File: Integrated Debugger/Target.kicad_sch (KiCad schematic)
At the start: 10 parts, among them J3 FPC socket 10P, J4 20021521-00010T1LF, Q1 DMN31D5UDA-7B, SW5 RESET, U3 TXB0106RGY

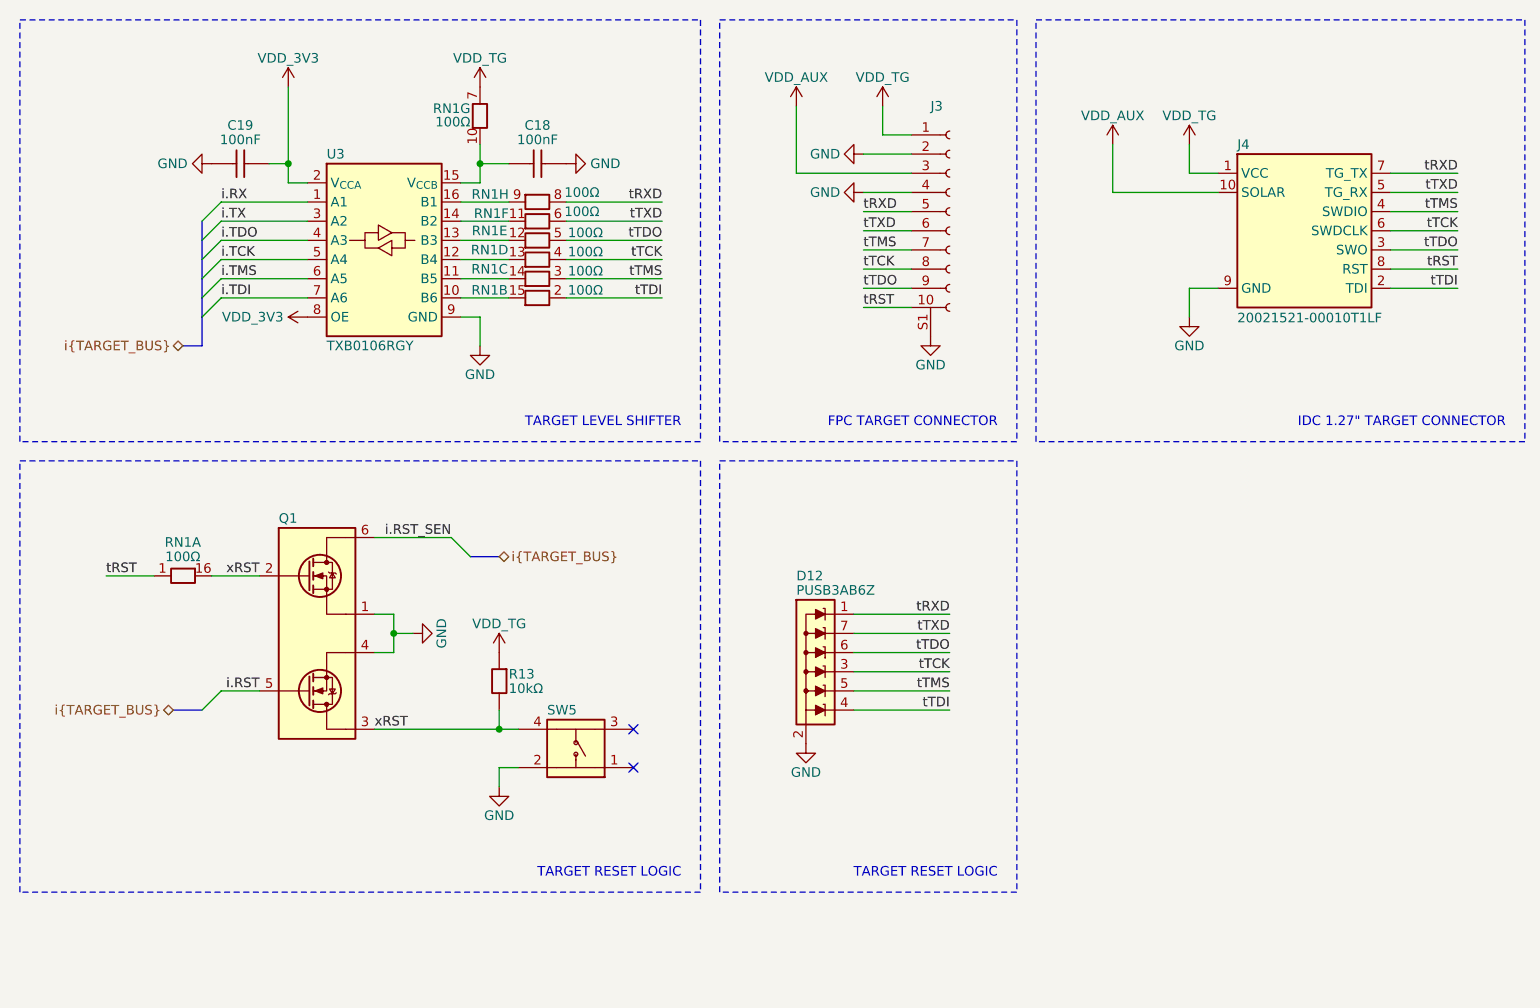
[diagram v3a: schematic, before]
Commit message: Reannotate schematic, update GND plane
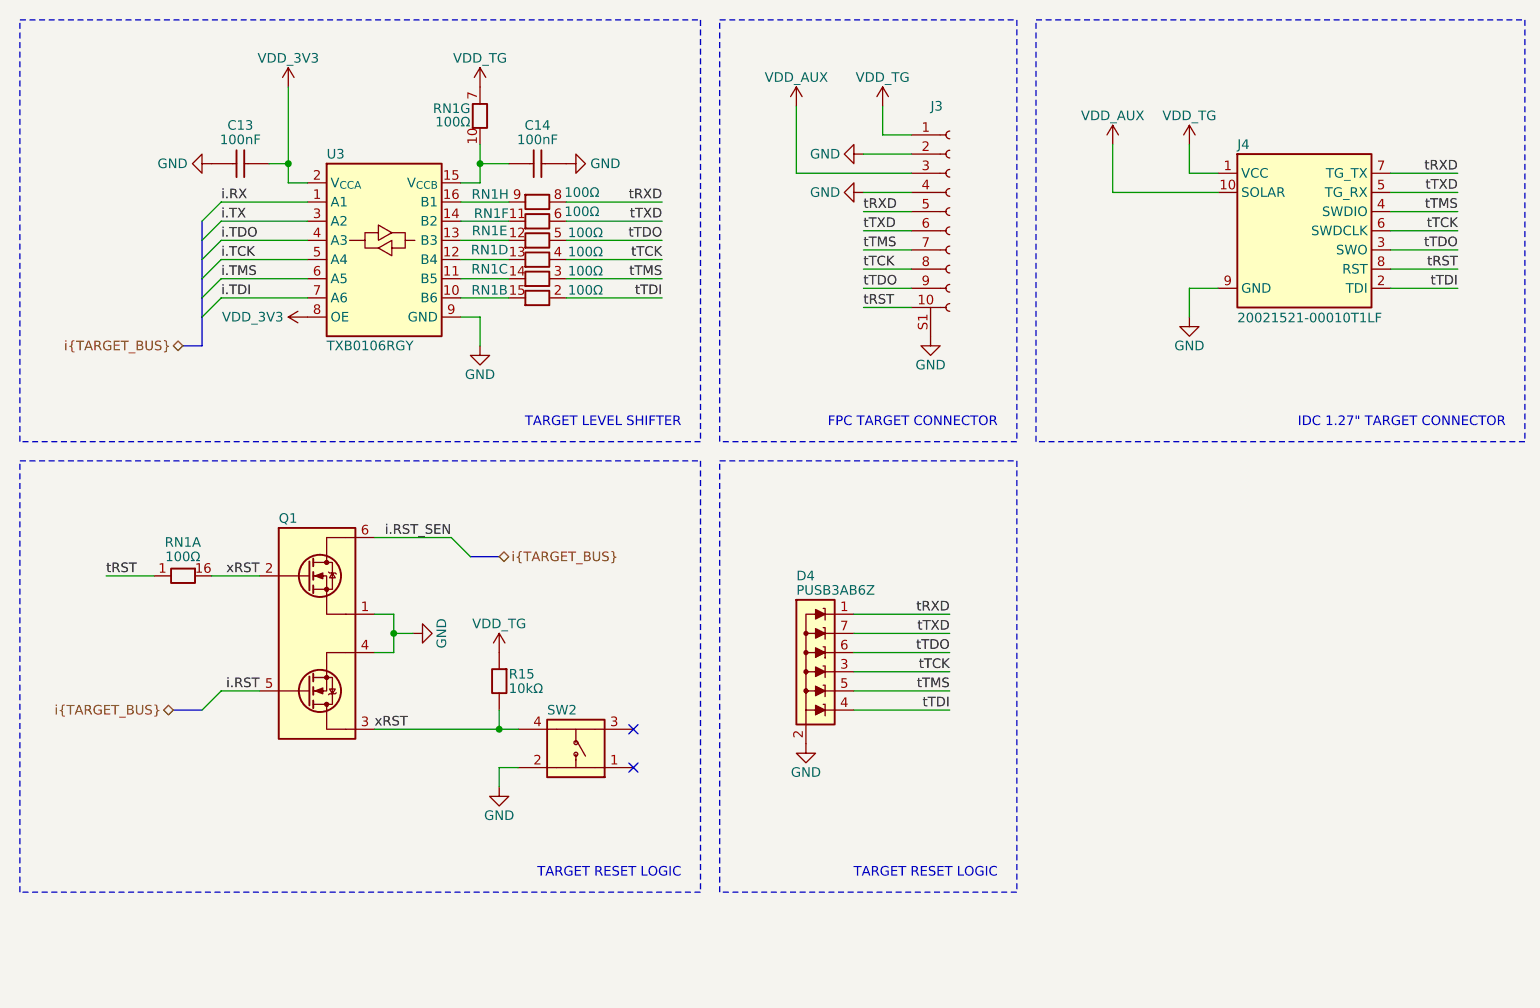
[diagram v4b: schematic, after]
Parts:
- renumbered C19 to C13, C18 to C14, D12 to D4, R13 to R15, SW5 to SW2
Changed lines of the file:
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@@
 		(dnp no)
 		(fields_autoplaced yes)
-		(property "Reference" "#PWR015"
+		(property "Reference" "#PWR039"
 			(at 66.04 54.61 0)
 			(effects
@@
 			(project "Integrated Debugger"
 				(path "/ce538ebe-fda9-4af3-9f8c-9fd5bf58f0e4/d9cee7b3-2b2b-4107-bac3-796b154ca54d"
-					(reference "#PWR015")
+					(reference "#PWR039")
 					(unit 1)
 				)
@@
 		(on_board yes)
 		(dnp no)
-		(property "Reference" "#PWR019"
+		(property "Reference" "#PWR043"
 			(at 107.95 20.32 0)
 			(effects
@@
 			(project "Integrated Debugger"
 				(path "/ce538ebe-fda9-4af3-9f8c-9fd5bf58f0e4/d9cee7b3-2b2b-4107-bac3-796b154ca54d"
-					(reference "#PWR019")
+					(reference "#PWR043")
 					(unit 1)
 				)
@@
 		(on_board yes)
 		(dnp no)
-		(property "Reference" "#PWR061"
+		(property "Reference" "#PWR045"
 			(at 110.49 22.86 0)
 			(effects
@@
 			(project "Integrated Debugger"
 				(path "/ce538ebe-fda9-4af3-9f8c-9fd5bf58f0e4/d9cee7b3-2b2b-4107-bac3-796b154ca54d"
-					(reference "#PWR061")
+					(reference "#PWR045")
 					(unit 1)
 				)
@@
 		(on_board yes)
 		(dnp no)
-		(property "Reference" "#PWR041"
+		(property "Reference" "#PWR038"
 			(at 66.04 17.78 0)
 			(effects
@@
 			(project "Integrated Debugger"
 				(path "/ce538ebe-fda9-4af3-9f8c-9fd5bf58f0e4/d9cee7b3-2b2b-4107-bac3-796b154ca54d"
-					(reference "#PWR041")
+					(reference "#PWR038")
 					(unit 1)
 				)
@@
 		(on_board yes)
 		(dnp no)
-		(property "Reference" "R13"
+		(property "Reference" "R15"
 			(at 69.85 91.7575 0)
 			(do_not_autoplace yes)
@@
 			(project "Integrated Debugger"
 				(path "/ce538ebe-fda9-4af3-9f8c-9fd5bf58f0e4/d9cee7b3-2b2b-4107-bac3-796b154ca54d"
-					(reference "R13")
+					(reference "R15")
 					(unit 1)
 				)
@@
 		(on_board yes)
 		(dnp no)
-		(property "Reference" "#PWR059"
+		(property "Reference" "#PWR034"
 			(at 24.13 24.13 0)
 			(effects
@@
 			(project "Integrated Debugger"
 				(path "/ce538ebe-fda9-4af3-9f8c-9fd5bf58f0e4/d9cee7b3-2b2b-4107-bac3-796b154ca54d"
-					(reference "#PWR059")
+					(reference "#PWR034")
 					(unit 1)
 				)
@@
 		(dnp no)
 		(fields_autoplaced yes)
-		(property "Reference" "#PWR017"
+		(property "Reference" "#PWR037"
 			(at 63.5 86.36 0)
 			(effects
@@
 			(project "Integrated Debugger"
 				(path "/ce538ebe-fda9-4af3-9f8c-9fd5bf58f0e4/d9cee7b3-2b2b-4107-bac3-796b154ca54d"
-					(reference "#PWR017")
+					(reference "#PWR037")
 					(unit 1)
 				)
@@
 		(on_board yes)
 		(dnp no)
-		(property "Reference" "#PWR024"
+		(property "Reference" "#PWR050"
 			(at 160.02 25.4 0)
 			(effects
@@
 			(project "Integrated Debugger"
 				(path "/ce538ebe-fda9-4af3-9f8c-9fd5bf58f0e4/d9cee7b3-2b2b-4107-bac3-796b154ca54d"
-					(reference "#PWR024")
+					(reference "#PWR050")
 					(unit 1)
 				)
@@
 		(on_board yes)
 		(dnp no)
-		(property "Reference" "#PWR055"
+		(property "Reference" "#PWR041"
 			(at 68.58 113.03 0)
 			(effects
@@
 			(project "Integrated Debugger"
 				(path "/ce538ebe-fda9-4af3-9f8c-9fd5bf58f0e4/d9cee7b3-2b2b-4107-bac3-796b154ca54d"
-					(reference "#PWR055")
+					(reference "#PWR041")
 					(unit 1)
 				)
@@
 		(dnp no)
 		(fields_autoplaced yes)
-		(property "Reference" "D12"
+		(property "Reference" "D4"
 			(at 107.95 78.74 0)
 			(do_not_autoplace yes)
@@
 			(project "Integrated Debugger"
 				(path "/ce538ebe-fda9-4af3-9f8c-9fd5bf58f0e4/d9cee7b3-2b2b-4107-bac3-796b154ca54d"
-					(reference "D12")
+					(reference "D4")
 					(unit 1)
 				)
@@
 		(on_board yes)
 		(dnp no)
-		(property "Reference" "#PWR025"
+		(property "Reference" "#PWR051"
 			(at 160.02 50.8 0)
 			(effects
@@
 			(project "Integrated Debugger"
 				(path "/ce538ebe-fda9-4af3-9f8c-9fd5bf58f0e4/d9cee7b3-2b2b-4107-bac3-796b154ca54d"
-					(reference "#PWR025")
+					(reference "#PWR051")
 					(unit 1)
 				)
@@
 		(on_board yes)
 		(dnp no)
-		(property "Reference" "#PWR023"
+		(property "Reference" "#PWR049"
 			(at 149.86 25.4 0)
 			(effects
@@
 			(project "Integrated Debugger"
 				(path "/ce538ebe-fda9-4af3-9f8c-9fd5bf58f0e4/d9cee7b3-2b2b-4107-bac3-796b154ca54d"
-					(reference "#PWR023")
+					(reference "#PWR049")
 					(unit 1)
 				)
@@
 		(on_board yes)
 		(dnp no)
-		(property "Reference" "C18"
+		(property "Reference" "C14"
 			(at 73.66 19.05 90)
 			(do_not_autoplace yes)
@@
 			(project "Integrated Debugger"
 				(path "/ce538ebe-fda9-4af3-9f8c-9fd5bf58f0e4/d9cee7b3-2b2b-4107-bac3-796b154ca54d"
-					(reference "C18")
+					(reference "C14")
 					(unit 1)
 				)
@@
 		(on_board yes)
 		(dnp no)
-		(property "Reference" "#PWR014"
+		(property "Reference" "#PWR035"
 			(at 40.64 17.78 0)
 			(effects
@@
 			(project "Integrated Debugger"
 				(path "/ce538ebe-fda9-4af3-9f8c-9fd5bf58f0e4/d9cee7b3-2b2b-4107-bac3-796b154ca54d"
-					(reference "#PWR014")
+					(reference "#PWR035")
 					(unit 1)
 				)
@@
 		(on_board yes)
 		(dnp no)
-		(property "Reference" "#PWR058"
+		(property "Reference" "#PWR042"
 			(at 83.82 24.13 0)
 			(effects
@@
 			(project "Integrated Debugger"
 				(path "/ce538ebe-fda9-4af3-9f8c-9fd5bf58f0e4/d9cee7b3-2b2b-4107-bac3-796b154ca54d"
-					(reference "#PWR058")
+					(reference "#PWR042")
 					(unit 1)
 				)
@@
 		(on_board yes)
 		(dnp no)
-		(property "Reference" "#PWR028"
+		(property "Reference" "#PWR044"
 			(at 109.22 107.315 0)
 			(effects
@@
 			(project "Integrated Debugger"
 				(path "/ce538ebe-fda9-4af3-9f8c-9fd5bf58f0e4/d9cee7b3-2b2b-4107-bac3-796b154ca54d"
-					(reference "#PWR028")
+					(reference "#PWR044")
 					(unit 1)
 				)
@@
 		(on_board yes)
 		(dnp no)
-		(property "Reference" "C19"
+		(property "Reference" "C13"
 			(at 34.29 19.05 90)
 			(do_not_autoplace yes)
@@
 			(project "Integrated Debugger"
 				(path "/ce538ebe-fda9-4af3-9f8c-9fd5bf58f0e4/d9cee7b3-2b2b-4107-bac3-796b154ca54d"
-					(reference "C19")
+					(reference "C13")
 					(unit 1)
 				)
@@
 		(on_board yes)
 		(dnp no)
-		(property "Reference" "#PWR021"
+		(property "Reference" "#PWR047"
 			(at 119.38 20.32 0)
 			(effects
@@
 			(project "Integrated Debugger"
 				(path "/ce538ebe-fda9-4af3-9f8c-9fd5bf58f0e4/d9cee7b3-2b2b-4107-bac3-796b154ca54d"
-					(reference "#PWR021")
+					(reference "#PWR047")
 					(unit 1)
 				)
@@
 		(on_board yes)
 		(dnp no)
-		(property "Reference" "#PWR064"
+		(property "Reference" "#PWR046"
 			(at 110.49 27.94 0)
 			(effects
@@
 			(project "Integrated Debugger"
 				(path "/ce538ebe-fda9-4af3-9f8c-9fd5bf58f0e4/d9cee7b3-2b2b-4107-bac3-796b154ca54d"
-					(reference "#PWR064")
+					(reference "#PWR046")
 					(unit 1)
 				)
@@
 		(on_board yes)
 		(dnp no)
-		(property "Reference" "#PWR057"
+		(property "Reference" "#PWR036"
 			(at 46.99 44.45 0)
 			(effects
@@
 			(project "Integrated Debugger"
 				(path "/ce538ebe-fda9-4af3-9f8c-9fd5bf58f0e4/d9cee7b3-2b2b-4107-bac3-796b154ca54d"
-					(reference "#PWR057")
+					(reference "#PWR036")
 					(unit 1)
 				)
@@
 		(on_board yes)
 		(dnp no)
-		(property "Reference" "#PWR022"
+		(property "Reference" "#PWR048"
 			(at 125.73 53.34 0)
 			(effects
@@
 			(project "Integrated Debugger"
 				(path "/ce538ebe-fda9-4af3-9f8c-9fd5bf58f0e4/d9cee7b3-2b2b-4107-bac3-796b154ca54d"
-					(reference "#PWR022")
+					(reference "#PWR048")
 					(unit 1)
 				)
@@
 		(on_board yes)
 		(dnp no)
-		(property "Reference" "#PWR018"
+		(property "Reference" "#PWR040"
 			(at 68.58 92.71 0)
 			(effects
@@
 			(project "Integrated Debugger"
 				(path "/ce538ebe-fda9-4af3-9f8c-9fd5bf58f0e4/d9cee7b3-2b2b-4107-bac3-796b154ca54d"
-					(reference "#PWR018")
+					(reference "#PWR040")
 					(unit 1)
 				)
@@
 		(on_board yes)
 		(dnp no)
-		(property "Reference" "SW5"
+		(property "Reference" "SW2"
 			(at 74.93 96.52 0)
 			(effects
@@
 			(project "Integrated Debugger"
 				(path "/ce538ebe-fda9-4af3-9f8c-9fd5bf58f0e4/d9cee7b3-2b2b-4107-bac3-796b154ca54d"
-					(reference "SW5")
+					(reference "SW2")
 					(unit 1)
 				)

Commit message: IDBG v2.0 production files
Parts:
- J4: LCSC Part # C2972785 -> C598547; MPN 20021521-00010T1LF -> 20021521-00010C1LF
- Q1: LCSC Part # C17642742 -> C2937136; MPN DMN31D5UDA-7B -> DMN2991UDA-7B
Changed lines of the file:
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@@
 			)
 		)
-		(property "MPN" "20021521-00010T1LF"
+		(property "MPN" "20021521-00010C1LF"
 			(at 175.26 49.53 0)
 			(effects
@@
 			)
 		)
-		(property "LCSC Part #" "C2972785"
+		(property "LCSC Part #" "C598547"
 			(at 175.26 51.435 0)
 			(effects
@@
 			)
 		)
-		(property "LCSC Part #" "C17642742"
+		(property "LCSC Part #" "C2937136"
 			(at 44.45 86.36 90)
 			(effects
@@
 			)
 		)
-		(property "MPN" "DMN31D5UDA-7B"
+		(property "MPN" "DMN2991UDA-7B"
 			(at 44.45 86.36 90)
 			(effects
